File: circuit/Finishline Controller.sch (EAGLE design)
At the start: 19 parts, among them IC1 74HCT245N, IC2 MAX3490ESA, X1 RJ45-6LC21-B

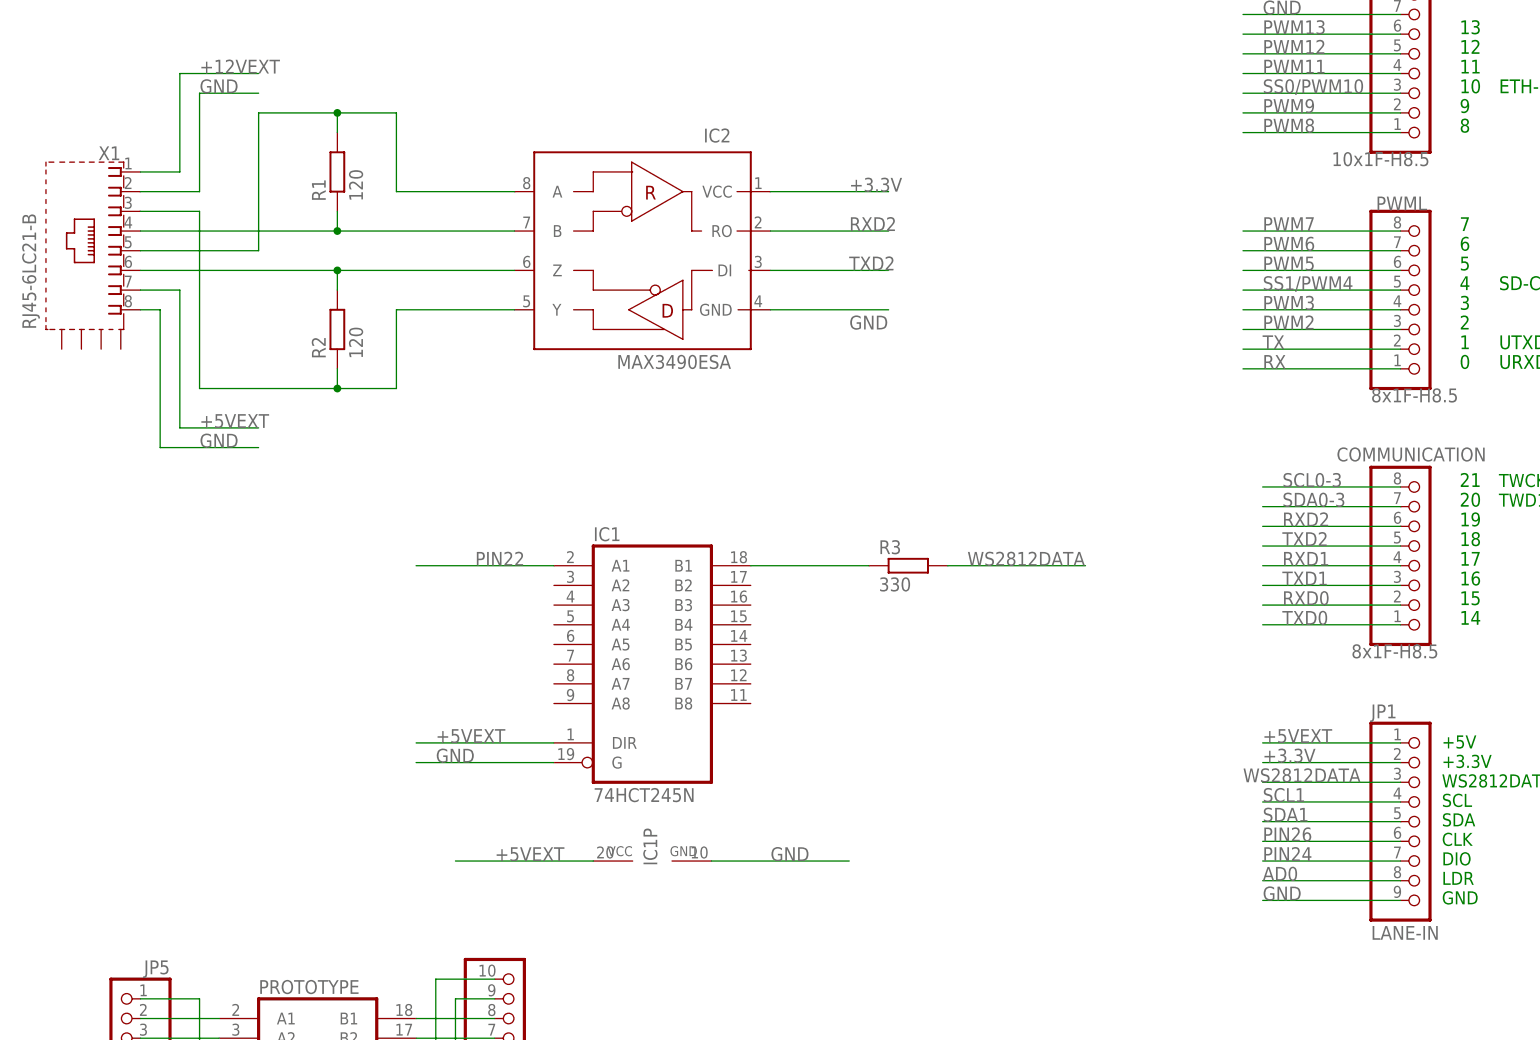
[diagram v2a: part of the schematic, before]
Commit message: finalize display module and controller shield
Display Module: Reordered the WS2813 LEDs to be consistent with normal
7-segment LED numbers (a-g). Changed schematics to be in the same
orientation as the board in top view. Re-adds the capacitors for the
WS2812 LEDs and the LDR line, which inadvertently got lost in the last
commit. Added silk screen.

Controller Shield: Added large electrolyte capacitor to buffer for the
WS2812 LEDs. Added a series resistor for the WS2812 data line. Added
silk screen and corrected wrong pinout of the I2C and serial header.
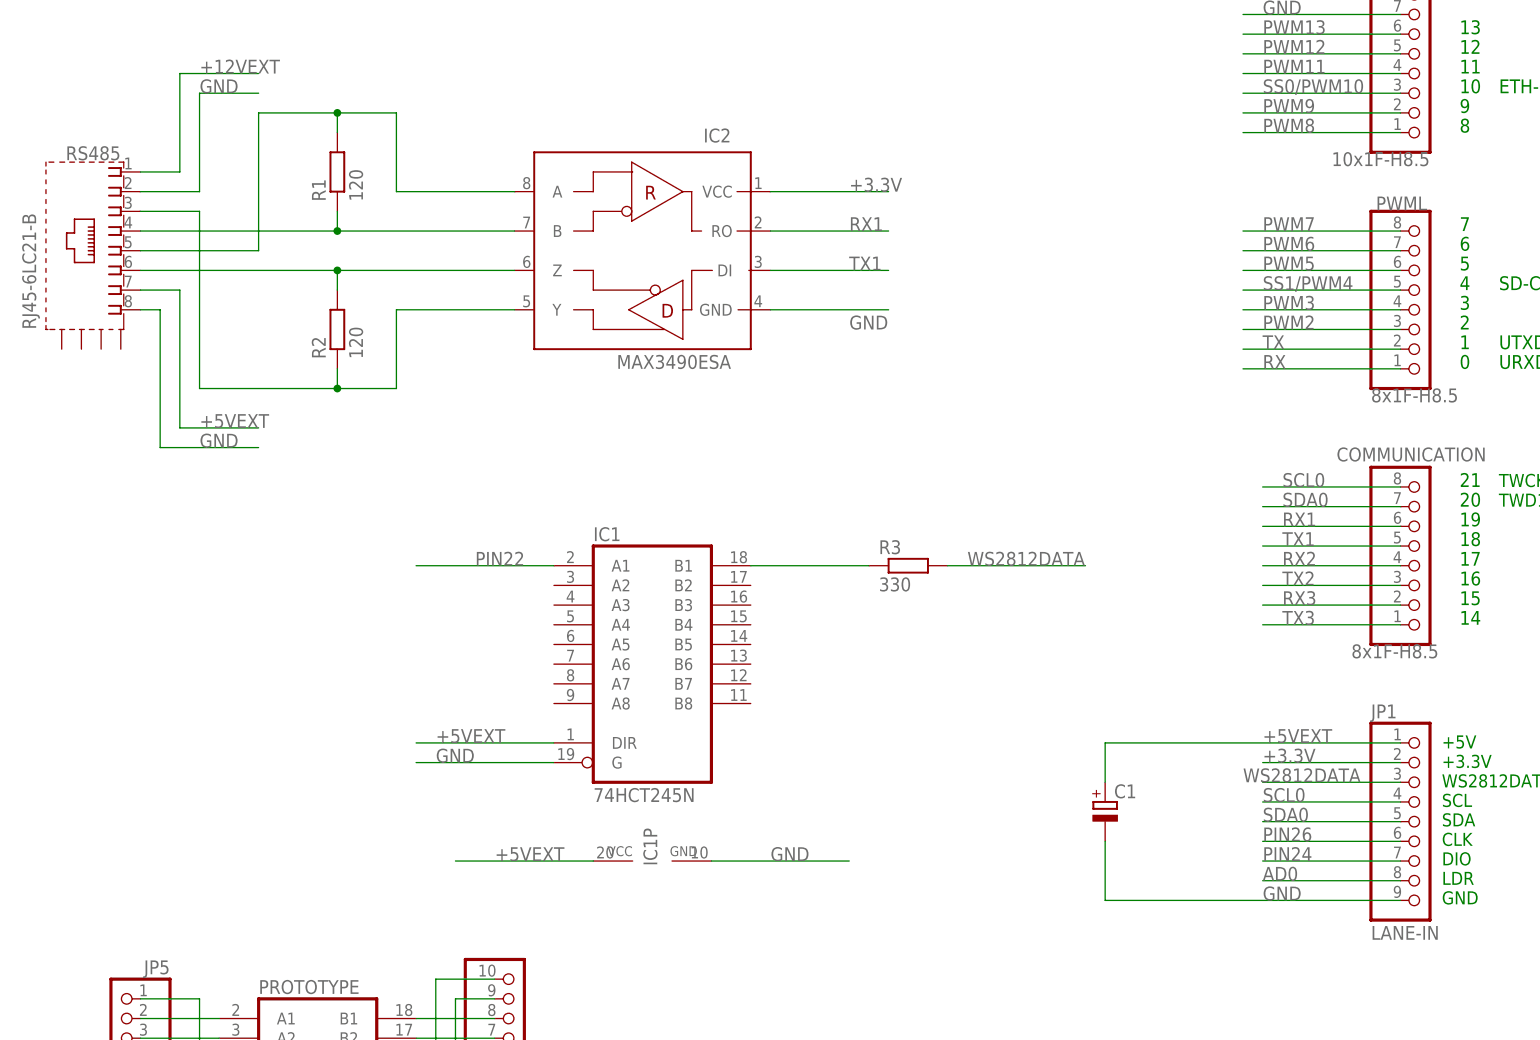
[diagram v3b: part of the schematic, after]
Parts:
- added C1: (no value), resistor:CPOL-EUE5-10.5
- renumbered X1 to RS485
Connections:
- net RXD0 renamed RX3
- net RXD1 renamed RX2
- net RXD2 renamed RX1
- net TXD0 renamed TX3
- net TXD1 renamed TX2
- net TXD2 renamed TX1
- removed net SCL0-3: COMMUNICATION.8
- removed net SDA0-3: COMMUNICATION.7
- new net SCL0: COMMUNICATION.8, JP1.4
- new net SDA0: COMMUNICATION.7, JP1.5
- net +5VEXT: now also C1.+
- net GND: now also C1.-
- net SCL1: no longer JP1.4
- net SDA1: no longer JP1.5
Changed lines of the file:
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@@
 <part name="IC1" library="74xx-eu" deviceset="74*245" device="N" technology="HCT"/>
 <part name="IC2" library="miro" deviceset="MAX3490" device="ESA"/>
-<part name="X1" library="con-tycoelectronics" deviceset="RJ45*2" device="1-B" technology="-6LC"/>
+<part name="RS485" library="con-tycoelectronics" deviceset="RJ45*2" device="1-B" technology="-6LC"/>
 <part name="R1" library="resistor" deviceset="R-EU_" device="R0805" value="120"/>
 <part name="R2" library="resistor" deviceset="R-EU_" device="R0805" value="120"/>
@@
 <part name="JP5" library="pinhead" deviceset="PINHD-1X10" device=""/>
 <part name="12V" library="con-ptr500" deviceset="AK300/2" device="" value="12V"/>
+<part name="C1" library="resistor" deviceset="CPOL-EU" device="E5-10.5"/>
 </parts>
 <sheets>
@@
 <instance part="IC1" gate="A" x="256.54" y="236.22"/>
 <instance part="IC2" gate="G$1" x="259.08" y="287.02" rot="MR0"/>
-<instance part="X1" gate="G$1" x="182.88" y="289.56" rot="MR0"/>
+<instance part="RS485" gate="G$1" x="182.88" y="289.56" rot="MR0"/>
 <instance part="R1" gate="G$1" x="215.9" y="299.72" rot="R90"/>
 <instance part="R2" gate="G$1" x="215.9" y="279.4" rot="R90"/>
@@
 <instance part="12V" gate="-1" x="469.9" y="256.54"/>
 <instance part="12V" gate="-2" x="469.9" y="251.46"/>
+<instance part="C1" gate="G$1" x="314.96" y="218.44"/>
 </instances>
 <busses>
@@
 <segment>
 <pinref part="JP1" gate="A" pin="9"/>
-<wire x1="353.06" y1="205.74" x2="335.28" y2="205.74" width="0.1524" layer="91"/>
 <label x="335.28" y="205.74" size="1.778" layer="95"/>
+<pinref part="C1" gate="G$1" pin="-"/>
+<wire x1="314.96" y1="213.36" x2="314.96" y2="205.74" width="0.1524" layer="91"/>
+<wire x1="314.96" y1="205.74" x2="353.06" y2="205.74" width="0.1524" layer="91"/>
 </segment>
 <segment>
@@
 </segment>
 <segment>
-<pinref part="X1" gate="G$1" pin="2"/>
+<pinref part="RS485" gate="G$1" pin="2"/>
 <wire x1="190.5" y1="297.18" x2="198.12" y2="297.18" width="0.1524" layer="91"/>
 <wire x1="198.12" y1="297.18" x2="198.12" y2="309.88" width="0.1524" layer="91"/>
@@
 </segment>
 <segment>
-<pinref part="X1" gate="G$1" pin="8"/>
+<pinref part="RS485" gate="G$1" pin="8"/>
 <wire x1="190.5" y1="281.94" x2="193.04" y2="281.94" width="0.1524" layer="91"/>
 <wire x1="193.04" y1="281.94" x2="193.04" y2="264.16" width="0.1524" layer="91"/>
@@
 </segment>
 </net>
-<net name="SCL0-3" class="0">
+<net name="SCL0" class="0">
 <segment>
 <wire x1="353.06" y1="259.08" x2="335.28" y2="259.08" width="0.1524" layer="91"/>
@@
 <pinref part="COMMUNICATION" gate="A" pin="8"/>
 </segment>
-</net>
-<net name="SDA0-3" class="0">
+<segment>
+<pinref part="JP1" gate="A" pin="4"/>
+<wire x1="353.06" y1="218.44" x2="335.28" y2="218.44" width="0.1524" layer="91"/>
+<label x="335.28" y="218.44" size="1.778" layer="95"/>
+</segment>
+</net>
+<net name="SDA0" class="0">
 <segment>
 <wire x1="335.28" y1="256.54" x2="353.06" y2="256.54" width="0.1524" layer="91"/>
@@
 <pinref part="COMMUNICATION" gate="A" pin="7"/>
 </segment>
-</net>
-<net name="RXD0" class="0">
+<segment>
+<pinref part="JP1" gate="A" pin="5"/>
+<wire x1="335.28" y1="215.9" x2="353.06" y2="215.9" width="0.1524" layer="91"/>
+<label x="335.28" y="215.9" size="1.778" layer="95"/>
+</segment>
+</net>
+<net name="RX3" class="0">
 <segment>
 <wire x1="335.28" y1="243.84" x2="353.06" y2="243.84" width="0.1524" layer="91"/>
@@
 </segment>
 </net>
-<net name="TXD0" class="0">
+<net name="TX3" class="0">
 <segment>
 <wire x1="335.28" y1="241.3" x2="353.06" y2="241.3" width="0.1524" layer="91"/>
@@
 </segment>
 </net>
-<net name="RXD1" class="0">
+<net name="RX2" class="0">
 <segment>
 <wire x1="335.28" y1="248.92" x2="353.06" y2="248.92" width="0.1524" layer="91"/>
@@
 </segment>
 </net>
-<net name="TXD1" class="0">
+<net name="TX2" class="0">
 <segment>
 <wire x1="335.28" y1="246.38" x2="353.06" y2="246.38" width="0.1524" layer="91"/>
@@
 </segment>
 </net>
-<net name="TXD2" class="0">
+<net name="TX1" class="0">
 <segment>
 <wire x1="335.28" y1="251.46" x2="353.06" y2="251.46" width="0.1524" layer="91"/>
@@
 <pinref part="PWMH" gate="A" pin="9"/>
 </segment>
-<segment>
-<pinref part="JP1" gate="A" pin="5"/>
-<wire x1="335.28" y1="215.9" x2="353.06" y2="215.9" width="0.1524" layer="91"/>
-<label x="335.28" y="215.9" size="1.778" layer="95"/>
-</segment>
 </net>
 <net name="SCL1" class="0">
@@
 <pinref part="PWMH" gate="A" pin="10"/>
 </segment>
-<segment>
-<pinref part="JP1" gate="A" pin="4"/>
-<wire x1="353.06" y1="218.44" x2="335.28" y2="218.44" width="0.1524" layer="91"/>
-<label x="335.28" y="218.44" size="1.778" layer="95"/>
-</segment>
 </net>
 <net name="SS1/PWM4" class="0">
@@
 </segment>
 </net>
-<net name="RXD2" class="0">
+<net name="RX1" class="0">
 <segment>
 <wire x1="335.28" y1="254" x2="353.06" y2="254" width="0.1524" layer="91"/>
@@
 <wire x1="215.9" y1="292.1" x2="215.9" y2="294.64" width="0.1524" layer="91"/>
 <junction x="215.9" y="292.1"/>
-<pinref part="X1" gate="G$1" pin="4"/>
+<pinref part="RS485" gate="G$1" pin="4"/>
 <wire x1="215.9" y1="292.1" x2="190.5" y2="292.1" width="0.1524" layer="91"/>
 </segment>
@@
 <wire x1="215.9" y1="287.02" x2="215.9" y2="284.48" width="0.1524" layer="91"/>
 <junction x="215.9" y="287.02"/>
-<pinref part="X1" gate="G$1" pin="6"/>
+<pinref part="RS485" gate="G$1" pin="6"/>
 <wire x1="190.5" y1="287.02" x2="215.9" y2="287.02" width="0.1524" layer="91"/>
 </segment>
@@
 <junction x="215.9" y="271.78"/>
 <wire x1="198.12" y1="271.78" x2="198.12" y2="294.64" width="0.1524" layer="91"/>
-<pinref part="X1" gate="G$1" pin="3"/>
+<pinref part="RS485" gate="G$1" pin="3"/>
 <wire x1="198.12" y1="294.64" x2="190.5" y2="294.64" width="0.1524" layer="91"/>
 </segment>
@@
 <pinref part="IC2" gate="G$1" pin="A"/>
 <wire x1="223.52" y1="297.18" x2="238.76" y2="297.18" width="0.1524" layer="91"/>
-<pinref part="X1" gate="G$1" pin="5"/>
+<pinref part="RS485" gate="G$1" pin="5"/>
 <wire x1="190.5" y1="289.56" x2="205.74" y2="289.56" width="0.1524" layer="91"/>
 <wire x1="205.74" y1="289.56" x2="205.74" y2="307.34" width="0.1524" layer="91"/>
@@
 <segment>
 <pinref part="JP1" gate="A" pin="1"/>
-<wire x1="335.28" y1="226.06" x2="353.06" y2="226.06" width="0.1524" layer="91"/>
 <label x="335.28" y="226.06" size="1.778" layer="95"/>
-</segment>
-<segment>
-<pinref part="X1" gate="G$1" pin="7"/>
+<pinref part="C1" gate="G$1" pin="+"/>
+<wire x1="314.96" y1="220.98" x2="314.96" y2="226.06" width="0.1524" layer="91"/>
+<wire x1="314.96" y1="226.06" x2="353.06" y2="226.06" width="0.1524" layer="91"/>
+</segment>
+<segment>
+<pinref part="RS485" gate="G$1" pin="7"/>
 <wire x1="190.5" y1="284.48" x2="195.58" y2="284.48" width="0.1524" layer="91"/>
 <wire x1="195.58" y1="284.48" x2="195.58" y2="266.7" width="0.1524" layer="91"/>
@@
 <net name="+12VEXT" class="0">
 <segment>
-<pinref part="X1" gate="G$1" pin="1"/>
+<pinref part="RS485" gate="G$1" pin="1"/>
 <wire x1="190.5" y1="299.72" x2="195.58" y2="299.72" width="0.1524" layer="91"/>
 <wire x1="195.58" y1="299.72" x2="195.58" y2="312.42" width="0.1524" layer="91"/>

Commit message: change the pin assignment for LDR and WS2812DATA
This uses a high power pin for the LED data and a normal analog pin for
the LDR line.
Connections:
- net AD0: no longer JP1.8
- net AD7: now also JP1.8
- net PIN22: no longer IC1A.A1
- net PIN28: now also IC1A.A1
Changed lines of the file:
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@@
 <pinref part="ADCL" gate="A" pin="8"/>
+</segment>
+<segment>
+<pinref part="JP1" gate="A" pin="8"/>
+<wire x1="353.06" y1="208.28" x2="335.28" y2="208.28" width="0.1524" layer="91"/>
+<label x="335.28" y="208.28" size="1.778" layer="95"/>
 </segment>
 </net>
@@
 <pinref part="ADCL" gate="A" pin="1"/>
 </segment>
-<segment>
-<pinref part="JP1" gate="A" pin="8"/>
-<wire x1="353.06" y1="208.28" x2="335.28" y2="208.28" width="0.1524" layer="91"/>
-<label x="335.28" y="208.28" size="1.778" layer="95"/>
-</segment>
 </net>
 <net name="AD8" class="0">
@@
 <pinref part="XIO" gate="A" pin="9"/>
 </segment>
+<segment>
+<pinref part="IC1" gate="A" pin="A1"/>
+<wire x1="243.84" y1="248.92" x2="226.06" y2="248.92" width="0.1524" layer="91"/>
+<label x="233.68" y="248.92" size="1.778" layer="95"/>
+</segment>
 </net>
 <net name="PIN26" class="0">
@@
 <pinref part="XIO" gate="A" pin="3"/>
 </segment>
-<segment>
-<pinref part="IC1" gate="A" pin="A1"/>
-<wire x1="243.84" y1="248.92" x2="226.06" y2="248.92" width="0.1524" layer="91"/>
-<label x="233.68" y="248.92" size="1.778" layer="95"/>
-</segment>
-</net>
+</net>

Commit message: correct some schematics mistakes and add gerber files
A demo mode button was added to the controller, the layout of the
controller shield as well as the startgate displays were changed.
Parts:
- added JP2: DEMO, pinhead:PINHD-1X2
- added JP3: RASPI, pinhead:PINHD-1X3
- added R4: 10K, resistor:R-EU_R0805
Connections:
- removed net +3.3V: IC2.VCC, JP1.2, POWER.2, POWER.4
- new net +3V3: IC2.VCC, JP1.2, POWER.2, POWER.4, R4.2
- net GND: now also JP2.2, JP3.3
- net PIN30: now also JP2.1, R4.1
- net RX2: now also JP3.1
- net TX2: now also JP3.2
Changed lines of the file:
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@@
 <part name="ADCL" library="SmartPrj" deviceset="PINHD-1X8" device="" value="8x1F-H8.5"/>
 <part name="COMMUNICATION" library="SmartPrj" deviceset="PINHD-1X8" device="" value="8x1F-H8.5"/>
-<part name="+3.3V" library="supply1" deviceset="+3V3" device=""/>
+<part name="+3V3" library="supply1" deviceset="+3V3" device=""/>
 <part name="ADCH" library="SmartPrj" deviceset="PINHD-1X8" device="" value="8x1F-H8.5"/>
 <part name="XIO" library="SmartPrj" deviceset="PINHD-2X18" device="" value="18x2F-H8.5"/>
@@
 <part name="12V" library="con-ptr500" deviceset="AK300/2" device="" value="12V"/>
 <part name="C1" library="resistor" deviceset="CPOL-EU" device="E5-10.5"/>
+<part name="R4" library="resistor" deviceset="R-EU_" device="R0805" value="10K"/>
+<part name="JP2" library="pinhead" deviceset="PINHD-1X2" device="" value="DEMO"/>
+<part name="GND1" library="supply1" deviceset="GND" device=""/>
+<part name="JP3" library="pinhead" deviceset="PINHD-1X3" device="" value="RASPI"/>
 </parts>
 <sheets>
@@
 <attribute name="VALUE" x="346.71" y="238.76" size="1.778" layer="96" rot="MR180"/>
 </instance>
-<instance part="+3.3V" gate="G$1" x="480.06" y="337.82" smashed="yes"/>
+<instance part="+3V3" gate="G$1" x="480.06" y="337.82" smashed="yes"/>
 <instance part="ADCH" gate="A" x="414.02" y="264.16" smashed="yes" rot="MR180">
 <attribute name="NAME" x="408.94" y="276.86" size="1.778" layer="95" rot="MR180"/>
@@
 <instance part="12V" gate="-2" x="469.9" y="251.46"/>
 <instance part="C1" gate="G$1" x="314.96" y="218.44"/>
+<instance part="R4" gate="G$1" x="180.34" y="243.84" rot="R90"/>
+<instance part="JP2" gate="G$1" x="190.5" y="220.98"/>
+<instance part="GND1" gate="1" x="180.34" y="210.82"/>
+<instance part="JP3" gate="A" x="314.96" y="177.8"/>
 </instances>
 <busses>
@@
 <label x="198.12" y="264.16" size="1.778" layer="95"/>
 </segment>
+<segment>
+<pinref part="GND1" gate="1" pin="GND"/>
+<pinref part="JP2" gate="G$1" pin="2"/>
+<wire x1="180.34" y1="213.36" x2="180.34" y2="220.98" width="0.1524" layer="91"/>
+<wire x1="180.34" y1="220.98" x2="187.96" y2="220.98" width="0.1524" layer="91"/>
+</segment>
+<segment>
+<pinref part="JP3" gate="A" pin="3"/>
+<wire x1="312.42" y1="175.26" x2="287.02" y2="175.26" width="0.1524" layer="91"/>
+<label x="294.64" y="175.26" size="1.778" layer="95"/>
+</segment>
 </net>
 <net name="VIN" class="0">
@@
 <pinref part="COMMUNICATION" gate="A" pin="4"/>
 </segment>
+<segment>
+<pinref part="JP3" gate="A" pin="1"/>
+<wire x1="312.42" y1="180.34" x2="287.02" y2="180.34" width="0.1524" layer="91"/>
+<label x="294.64" y="180.34" size="1.778" layer="95"/>
+</segment>
 </net>
 <net name="TX2" class="0">
@@
 <pinref part="COMMUNICATION" gate="A" pin="3"/>
 </segment>
+<segment>
+<pinref part="JP3" gate="A" pin="2"/>
+<wire x1="312.42" y1="177.8" x2="287.02" y2="177.8" width="0.1524" layer="91"/>
+<label x="294.64" y="177.8" size="1.778" layer="95"/>
+</segment>
 </net>
 <net name="TX1" class="0">
@@
 <label x="421.64" y="307.34" size="1.778" layer="95"/>
 <pinref part="XIO" gate="A" pin="11"/>
+</segment>
+<segment>
+<pinref part="R4" gate="G$1" pin="1"/>
+<wire x1="180.34" y1="238.76" x2="180.34" y2="233.68" width="0.1524" layer="91"/>
+<pinref part="JP2" gate="G$1" pin="1"/>
+<wire x1="180.34" y1="233.68" x2="180.34" y2="223.52" width="0.1524" layer="91"/>
+<wire x1="187.96" y1="223.52" x2="180.34" y2="223.52" width="0.1524" layer="91"/>
+<wire x1="180.34" y1="233.68" x2="203.2" y2="233.68" width="0.1524" layer="91"/>
+<junction x="180.34" y="233.68"/>
+<label x="190.5" y="233.68" size="1.778" layer="95"/>
 </segment>
 </net>
@@
 </segment>
 </net>
-<net name="+3.3V" class="0">
-<segment>
-<pinref part="IC2" gate="G$1" pin="VCC"/>
-<wire x1="271.78" y1="297.18" x2="287.02" y2="297.18" width="0.1524" layer="91"/>
-<label x="281.94" y="297.18" size="1.778" layer="95"/>
-</segment>
-<segment>
-<wire x1="495.3" y1="322.58" x2="485.14" y2="322.58" width="0.1524" layer="91"/>
-<wire x1="485.14" y1="322.58" x2="480.06" y2="322.58" width="0.1524" layer="91"/>
-<wire x1="480.06" y1="322.58" x2="480.06" y2="335.28" width="0.1524" layer="91"/>
-<wire x1="495.3" y1="327.66" x2="485.14" y2="327.66" width="0.1524" layer="91"/>
-<wire x1="485.14" y1="327.66" x2="485.14" y2="322.58" width="0.1524" layer="91"/>
-<junction x="485.14" y="322.58"/>
-<pinref part="+3.3V" gate="G$1" pin="+3V3"/>
-<pinref part="POWER" gate="A" pin="4"/>
-<pinref part="POWER" gate="A" pin="2"/>
-<label x="477.52" y="340.36" size="1.778" layer="95"/>
-</segment>
-<segment>
-<pinref part="JP1" gate="A" pin="2"/>
-<wire x1="353.06" y1="223.52" x2="335.28" y2="223.52" width="0.1524" layer="91"/>
-<label x="335.28" y="223.52" size="1.778" layer="95"/>
-</segment>
-</net>
 <net name="+5VEXT" class="0">
 <segment>
@@
 </segment>
 </net>
+<net name="+3V3" class="0">
+<segment>
+<pinref part="R4" gate="G$1" pin="2"/>
+<wire x1="180.34" y1="248.92" x2="180.34" y2="259.08" width="0.1524" layer="91"/>
+<label x="180.34" y="251.46" size="1.778" layer="95" rot="R90"/>
+</segment>
+<segment>
+<pinref part="IC2" gate="G$1" pin="VCC"/>
+<wire x1="271.78" y1="297.18" x2="287.02" y2="297.18" width="0.1524" layer="91"/>
+<label x="281.94" y="297.18" size="1.778" layer="95"/>
+</segment>
+<segment>
+<wire x1="495.3" y1="322.58" x2="485.14" y2="322.58" width="0.1524" layer="91"/>
+<wire x1="485.14" y1="322.58" x2="480.06" y2="322.58" width="0.1524" layer="91"/>
+<wire x1="480.06" y1="322.58" x2="480.06" y2="335.28" width="0.1524" layer="91"/>
+<wire x1="495.3" y1="327.66" x2="485.14" y2="327.66" width="0.1524" layer="91"/>
+<wire x1="485.14" y1="327.66" x2="485.14" y2="322.58" width="0.1524" layer="91"/>
+<junction x="485.14" y="322.58"/>
+<pinref part="+3V3" gate="G$1" pin="+3V3"/>
+<pinref part="POWER" gate="A" pin="4"/>
+<pinref part="POWER" gate="A" pin="2"/>
+<label x="477.52" y="340.36" size="1.778" layer="95"/>
+</segment>
+<segment>
+<pinref part="JP1" gate="A" pin="2"/>
+<wire x1="353.06" y1="223.52" x2="335.28" y2="223.52" width="0.1524" layer="91"/>
+<label x="335.28" y="223.52" size="1.778" layer="95"/>
+</segment>
+</net>
